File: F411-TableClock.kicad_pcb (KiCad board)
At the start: 2 copper layers, 81 x 89.1 mm, 45 parts, among them J1 USB_C_Receptacle_USB2.0_16P, J2 Conn_01x16_Socket, J3 Conn_01x04_Pin, J4 Conn_01x09_Socket, J5 Conn_01x09_Socket, Q1 DMG3415U, Q2 BC547, SW1 SW_Push, SW2 SW_Push, SW3 SW_Push, SW4 SW_Push, U1 STM32F411CCUx, U2 AP2204K-3.3, U3 AM2302, Y1 Crystal

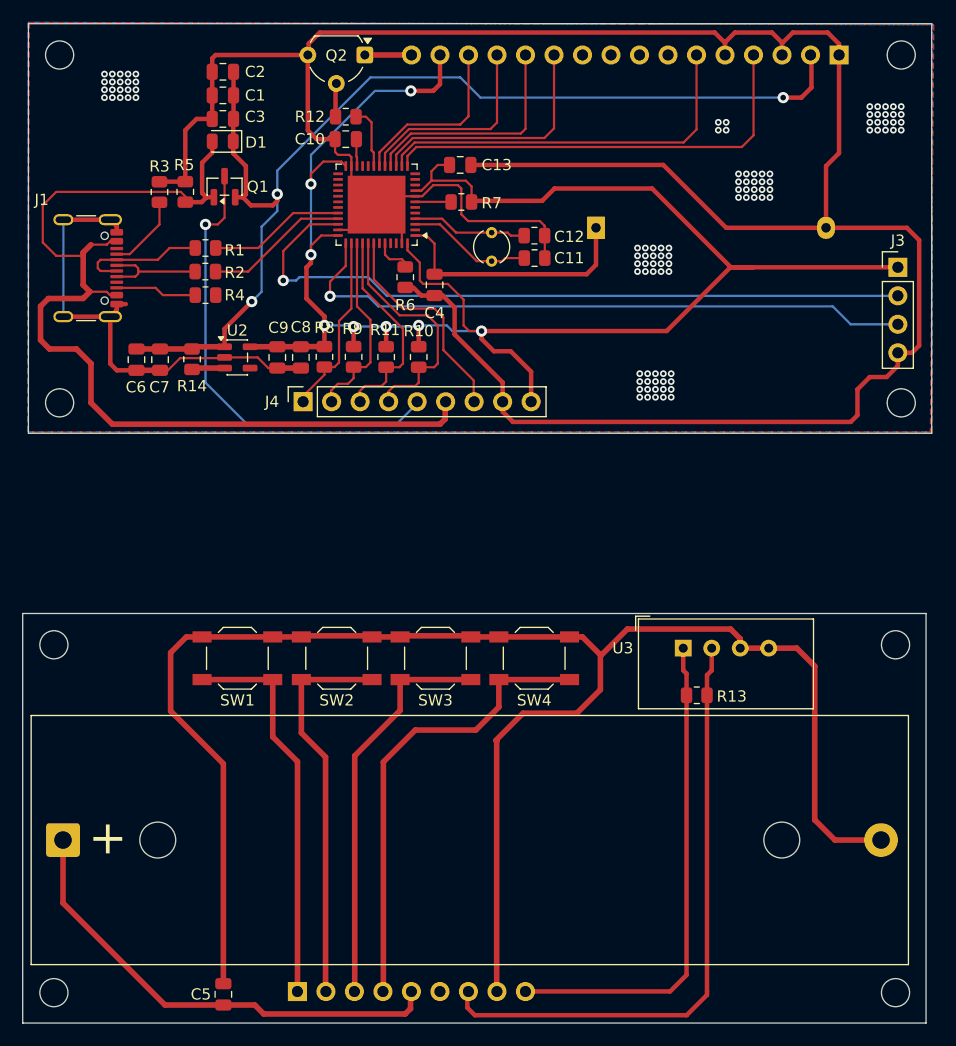
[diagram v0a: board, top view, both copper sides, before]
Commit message: Add positions CSV file for component placement in production
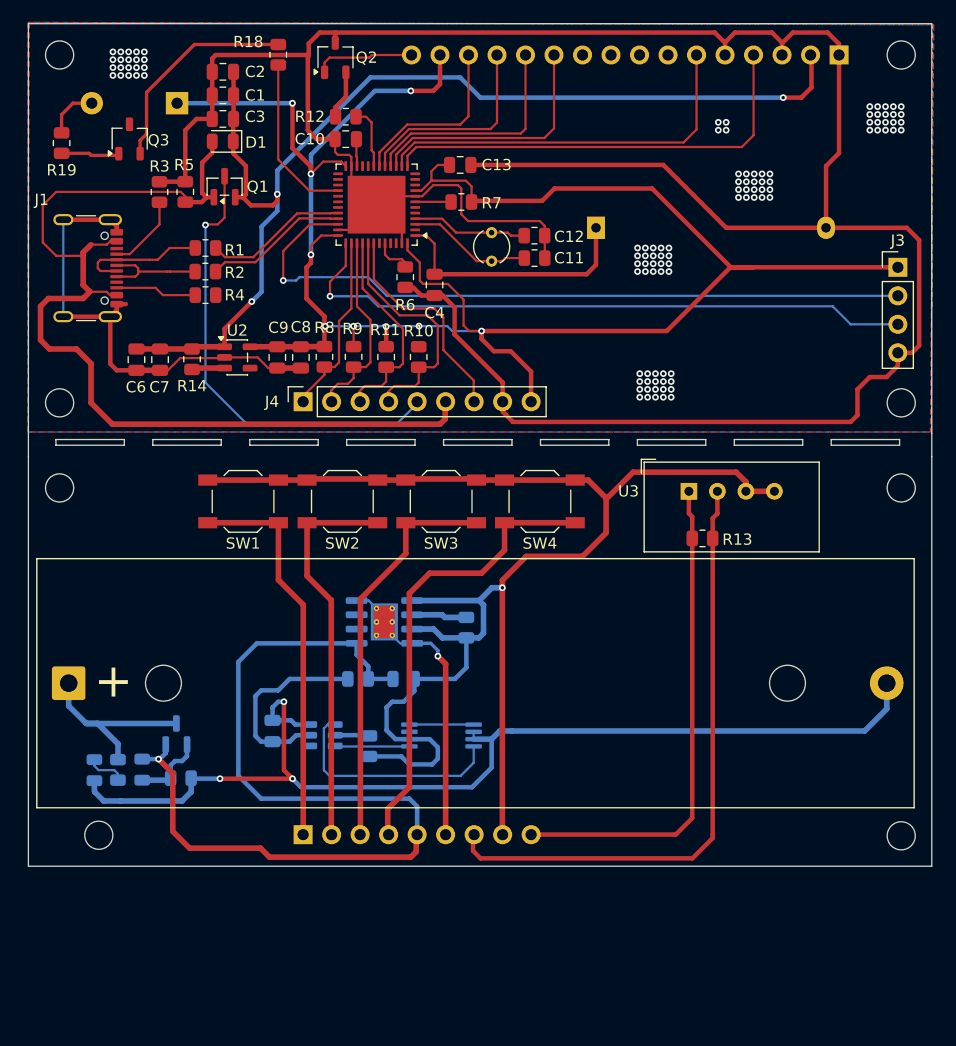
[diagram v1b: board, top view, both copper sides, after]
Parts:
- removed C5: 10uf, Capacitor_SMD:C_0805_2012Metric
- added BZ1: Buzzer, Buzzer_Beeper:Buzzer_12x9.5RM7.6, B.Cu at (104.3, 56.9)
- added C14: 10uf, Capacitor_SMD:C_0805_2012Metric, B.Cu at (124.5, 108.2)
- added C15: 100nf, Capacitor_SMD:C_0805_2012Metric, B.Cu at (112.8, 112.8)
- added D2: 1N5819, Diode_SMD:D_0805_2012Metric, B.Cu at (101.2, 116.3)
- added D3: LED, LED_SMD:LED_0805_2012Metric, B.Cu at (96.9, 116.3)
- added Q3: BC547, Package_TO_SOT_SMD:TSOT-23, F.Cu at (100.0, 60.1)
- added Q4: FS8205A, Package_SO:TSSOP-8_4.4x3mm_P0.65mm, B.Cu at (127.8, 113.2)
- added Q5: DMG3415U, Package_TO_SOT_SMD:SOT-23, B.Cu at (104.2, 113.1)
- added R15: 10k, Resistor_SMD:R_0805_2012Metric, B.Cu at (130.0, 103.6)
- added R16: 1k, Resistor_SMD:R_0805_2012Metric, B.Cu at (121.4, 114.2)
- added R17: 100E, Resistor_SMD:R_0805_2012Metric, B.Cu at (120.4, 108.2)
- added R18: 10k, Resistor_SMD:R_0805_2012Metric, F.Cu at (113.3, 52.6)
- added R19: 10k, Resistor_SMD:R_0805_2012Metric, F.Cu at (94.0, 60.5)
- added R20: 10k, Resistor_SMD:R_0805_2012Metric, B.Cu at (104.6, 117.0)
- added R21: 10k, Resistor_SMD:R_0805_2012Metric, B.Cu at (99.0, 116.3)
- added U4: TP4056-42-ESOP8, Package_SO:SOIC-8-1EP_3.9x4.9mm_P1.27mm_EP2.41x3.3mm_ThermalVias, B.Cu at (122.7, 103.1)
- added U5: DW01A, Package_TO_SOT_SMD:SOT-23-6, B.Cu at (117.2, 113.2)
- Q2: footprint Package_TO_SOT_THT:TO-92L_Wide -> Package_TO_SOT_SMD:TSOT-23
- moved BT1 14.0 mm to (94.6, 108.6)
- moved J5 14.0 mm to (115.5, 122.1)
- moved R13 14.0 mm to (151.1, 95.7)
- moved SW1 14.0 mm to (110.2, 92.4)
- moved SW2 14.0 mm to (119.0, 92.4)
- moved SW3 14.0 mm to (127.8, 92.4)
- moved SW4 14.0 mm to (136.6, 92.4)
- moved U3 14.0 mm to (149.9, 91.5)
- moved Q2 2.65 mm to (118.4, 52.8), turned to 90 degrees
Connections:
- BT1 pad 1: +BATT_1 -> Net-(BT1-+)
- BT1 pad 2: GND_1 -> BAT_GND
- U1 pad 28: unconnected-(U1-PB15-Pad28) -> /BUZZ
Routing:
- net BAT_GND: track 0.00 -> 96.7 mm, vias 0 -> 3
- net +BATT_1: track 42.2 -> 81.4 mm, vias 0 -> 1
- net +5V_1: track 0.00 -> 31.5 mm, vias 0 -> 1
- net Net-(U5-OD): track 0.00 -> 20.4 mm
- net Net-(Q3-B): track 0.00 -> 19.2 mm
- net Net-(U5-VCC): track 0.00 -> 17.7 mm
- net Net-(BT1-+): track 0.00 -> 17.3 mm
- net /BUZZ: track 0.00 -> 14.9 mm
- net +3.3V: track 168.4 -> 183.1 mm, vias 8 -> 9
- net GND_1: track 150.2 -> 136.1 mm, vias 0 -> 1
- net Net-(U5-OC): track 0.00 -> 6.62 mm
- net Net-(D2-A): track 0.00 -> 6.59 mm
- net Net-(Q4-Pad1): track 0.00 -> 5.73 mm
- net Net-(Q3-C): track 0.00 -> 5.22 mm
- net Net-(U4-PROG): track 0.00 -> 4.92 mm
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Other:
- board size 81 x 89.1 mm -> 80.5 x 75.1 mm
